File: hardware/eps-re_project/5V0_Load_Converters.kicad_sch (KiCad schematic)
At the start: 73 parts, among them Q10 EPC2016C, Q11 EPC2016C, Q12 EPC2016C, Q7 SI2302, Q8 SI2302, Q9 EPC2016C, U24 INA199C3DCKR

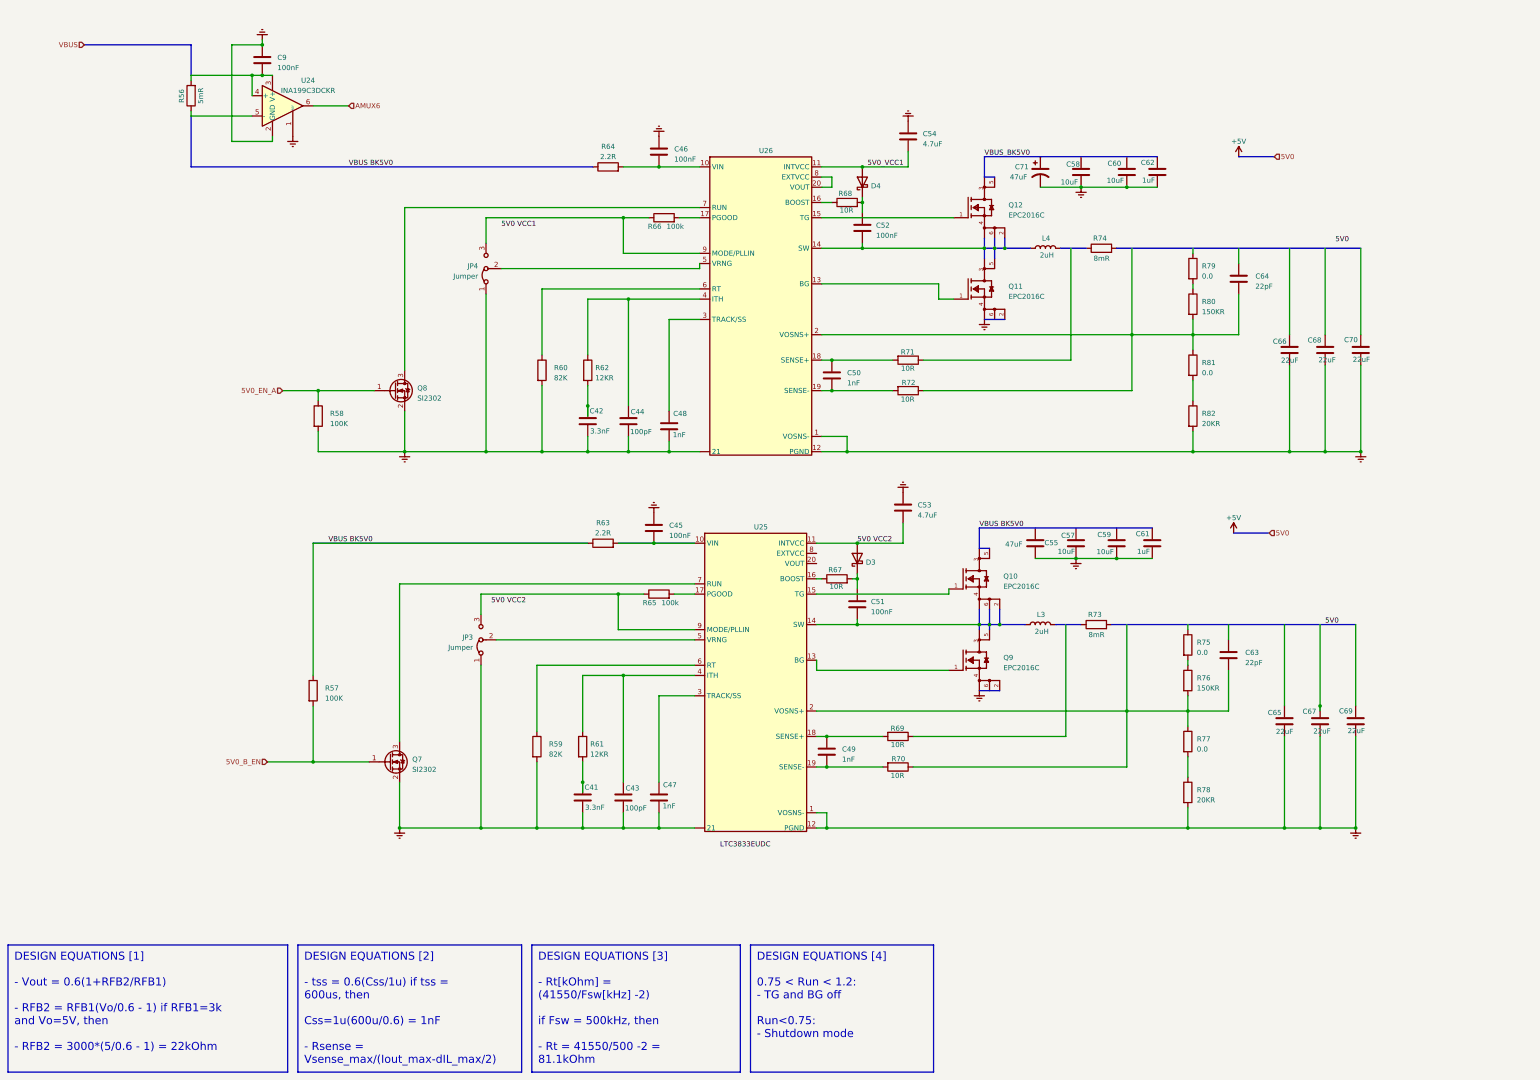
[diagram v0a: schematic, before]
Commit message: hardware: Restructuring the circuit, modifying symbols, footprints and other corrections
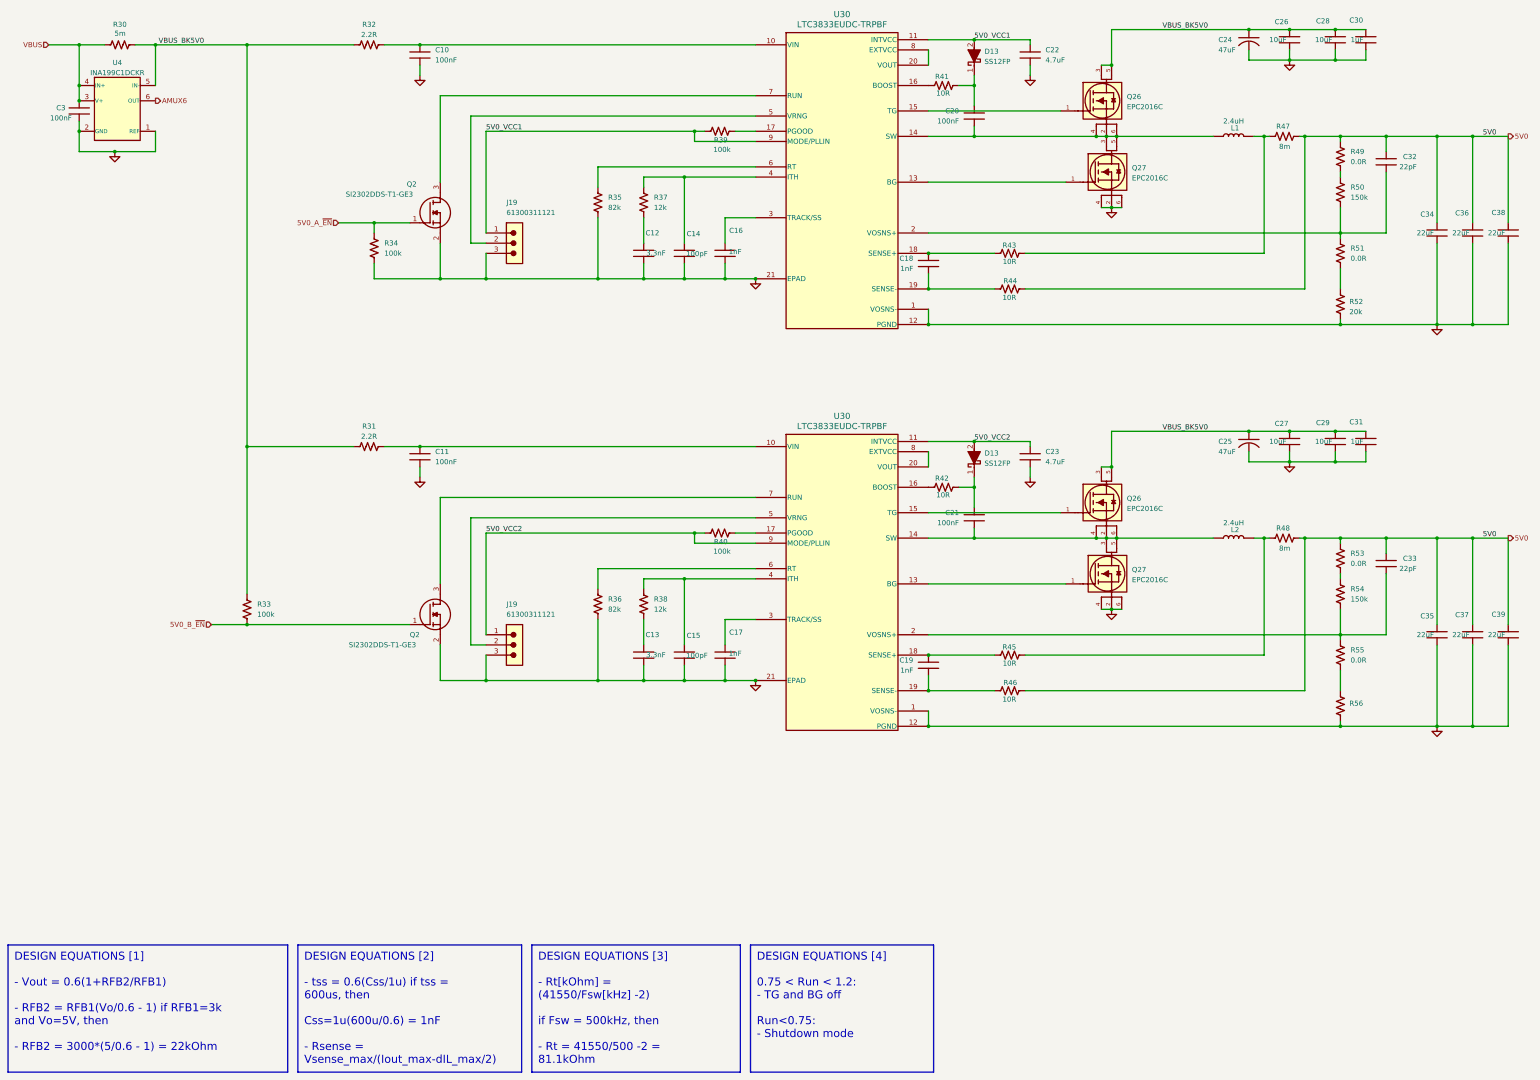
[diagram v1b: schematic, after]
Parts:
- removed C41, C42: 3.3nF, symbol Device:C
- removed C43, C44: 100pF, symbol Device:C
- removed C45, C46, C51, C52, C9: 100nF, symbol Device:C
- removed C47, C48, C49, C50: 1nF, symbol Device:C
- removed C53, C54: 4.7uF, symbol Device:C
- removed C55: 47uF, symbol Device:C
- removed C57, C58, C59, C60: 10uF, symbol Device:C
- removed C61, C62: 1uF, symbol Device:C
- removed C63, C64: 22pF, symbol Device:C
- removed C65, C66, C67, C68, C69, C70: 22uF, symbol Device:C
- removed C71: 47uF, symbol Device:C_Polarized_US
- removed D3, D4: ~, symbol Device:D_Schottky
- removed JP3, JP4: Jumper, symbol Jumper:Jumper_3_Bridged12
- removed L3, L4: 2uH, symbol Device:L
- removed Q10, Q11, Q12, Q9: EPC2016C, EPC-EPC2016C-*, symbol eec:EPC2016C
- removed Q7, Q8: SI2302, symbol Device:Q_NMOS_GSD
- removed R56: 5mR, symbol Device:R
- removed R57, R58: 100K, symbol Device:R
- removed R59, R60: 82K, symbol Device:R
- removed R61, R62: 12KR, symbol Device:R
- removed R63, R64: 2.2R, symbol Device:R
- removed R65, R66: 100k, symbol Device:R
- removed R67, R68, R69, R70, R71, R72: 10R, symbol Device:R
- removed R73, R74: 8mR, symbol Device:R
- removed R75, R77, R79, R81: 0.0, symbol Device:R
- removed R76, R80: 150KR, symbol Device:R
- removed R78, R82: 20KR, symbol Device:R
- removed U24: INA199C3DCKR, Package_TO_SOT_SMD:SOT-363_SC-70-6, symbol Amplifier_Current:INA199xxDCK
- removed U25, U26: ~, symbol New_Library:LTC3833EUDC
- added C10, C11, C20, C21, C3: 100nF, footprints:C0603C104K5RACTU, symbol C0603C104K5RACTU:C0603C104K5RACTU
- added C12, C13: 3.3nF, footprints:C0603C332J5GACAUTO, symbol C0603C332J5GACAUTO:C0603C332J5GACAUTO
- added C14, C15: 100pF, footprints:C0603C101J5GACAUTO, symbol C0603C101J5GACAUTO:C0603C101J5GACAUTO
- added C16, C17, C18, C19: 1nF, footprints:C0603C102F3GACTU, symbol C0603C102F3GACTU:C0603C102F3GACTU
- added C22, C23: 4.7uF, footprints:GCM32ER71H475KA55L, symbol GCM32ER71H475KA55L:GCM32ER71H475KA55L
- added C24, C25: 47uF, footprints:T495X476K035ATE300, symbol T495X476K035ATE300:T495X476K035ATE300
- added C26, C27, C28, C29: 10uF, footprints:C1210C106K5RACTU, symbol C1210C106K5RACTU:C1210C106K5RACTU
- added C30, C31: 1uF, footprints:C0805C105K5RACTU, symbol C0805C105K5RACTU:C0805C105K5RACTU
- added C32, C33: 22pF, footprints:C0603C220K5RACAUTO, symbol C0603C220K5RACAUTO:C0603C220K5RACAUTO
- added C34, C35, C36, C37, C38, C39: 22uF, footprints:GCM32ER71C226KE19L, symbol GCM32ER71C226KE19L:GCM32ER71C226KE19L
- added D13 (x2): SS12FP, footprints:SS12FP, symbol SS12FP:SS12FP
- added J19 (x2): 61300311121, footprints:61300311121, symbol 61300311121:61300311121
- added L1, L2: 2.4uH, footprints:744325240, symbol 744325240:744325240
- added Q2 (x2): SI2302DDS-T1-GE3, footprints:SI2302DDS-T1-GE3, symbol SI2302DDS-T1-GE3:SI2302DDS-T1-GE3
- added Q26 (x2), Q27 (x2): EPC2016C, footprints:EPC2016C, symbol EPC2016C:EPC2016C
- added R30: 5m, symbol Device:R_US
- added R31, R32: 2.2R, symbol Device:R_US
- added R33, R34, R39, R40: 100k, symbol Device:R_US
- added R35, R36: 82k, symbol Device:R_US
- added R37, R38: 12k, symbol Device:R_US
- added R41, R42, R43, R44, R45, R46: 10R, symbol Device:R_US
- added R47, R48: 8m, symbol Device:R_US
- added R49, R51, R53, R55: 0.0R, symbol Device:R_US
- added R50, R54: 150k, symbol Device:R_US
- added R52, R56: 20k, symbol Device:R_US
- added U30 (x2): LTC3833EUDC-TRPBF, footprints:LTC3833EUDC#TRPBF, symbol LTC3833EUDC#TRPBF:LTC3833EUDC-TRPBF
- added U4: INA199C1DCKR, footprints:INA199C1DCKR, symbol INA199C1DCKR:INA199xxDCK
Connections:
- net 5V0: now also C32.1, C33.1, C34.2, C35.2, C36.2, C37.2, C38.2, C39.2, R44.1, R46.1, R47.2, R48.2, R49.1, R53.1
- net 5V0_VCC1: now also C22.1, D13.2 (A), J19.1, R39.1, U30.11 (INTVCC), U30.9 (MODE/PLLIN)
- net AMUX6: now also U4.6 (OUT)
- net VBUS: now also C3.1, R30.1, U4.3 (V+), U4.4 (IN+)
- net VBUS_BK5V0: now also C24.2 (ANODE), C25.2 (ANODE), C26.1, C27.1, C28.1, C29.1, C30.1, C31.1, Q26.3 (Drain), Q26.3 (Drain), Q26.5 (Drain), Q26.5 (Drain), R30.2, R31.1, R32.1, R33.1, U4.5 (IN-)
- new net: C32.2, R50.2, R51.1, U30.2 (VOSNS+)
- new net: R51.2, R52.1
- new net: L1.2, R43.1, R47.1
- new net: L2.2, R45.1, R48.1
- new net: C11.2, R31.2, U30.10 (VIN)
- new net: Q27.1 (Gate), U30.13 (BG) (x2)
- new net: C21.2, L2.1, Q26.2 (Substrate), Q26.4 (Source), Q26.6 (Source), Q27.3 (Drain), Q27.5 (Drain), U30.14 (SW)
- new net: Q26.1 (Gate), U30.15 (TG) (x2)
- new net: R42.1, U30.16 (BOOST)
- new net: R40.2, U30.17 (PGOOD)
- new net: C19.1, R45.2, U30.18 (SENSE+)
- new net: C19.2, R46.2, U30.19 (SENSE-)
- new net: C33.2, R54.2, R55.1, U30.2 (VOSNS+)
- new net: U30.20 (VOUT), U30.8 (EXTVCC) (x2)
- new net: C17.1, U30.3 (TRACK/SS)
- new net: C15.1, R38.1, U30.4 (ITH)
- new net: J19.2, U30.5 (VRNG) (x2)
- new net: R36.1, U30.6 (RT)
- new net: Q2.3 (D), U30.7 (RUN) (x2)
- new net: C20.2, L1.1, Q26.2 (Substrate), Q26.4 (Source), Q26.6 (Source), Q27.3 (Drain), Q27.5 (Drain), U30.14 (SW)
- new net: C16.1, U30.3 (TRACK/SS)
- new net: C10.2, R32.2, U30.10 (VIN)
- new net: C18.2, R44.2, U30.19 (SENSE-)
- new net: C18.1, R43.2, U30.18 (SENSE+)
- new net: R55.2, R56.1
- new net: R49.2, R50.1
- new net: C13.1, R38.2
- new net: R39.2, U30.17 (PGOOD)
- new net: C21.1, D13.1 (K), R42.2
- new net: R53.2, R54.1
- new net: C20.1, D13.1 (K), R41.2
- new net: R41.1, U30.16 (BOOST)
- new net: C14.1, R37.1, U30.4 (ITH)
- new net: R35.1, U30.6 (RT)
- new net: C12.1, R37.2
- new net 5V0_A_~{EN}: Q2.1 (G), R34.1
- new net 5V0_B_~{EN}: Q2.1 (G), R33.2
- new net 5V0_VCC2: C23.1, D13.2 (A), J19.1, R40.1, U30.11 (INTVCC), U30.9 (MODE/PLLIN)
- new net GND: C10.1, C11.1, C12.2, C13.2, C14.2, C15.2, C16.2, C17.2, C22.2, C23.2, C24.1 (CATHODE), C25.1 (CATHODE), C26.2, C27.2, C28.2, C29.2, C3.2, C30.2, C31.2, C34.1, C35.1, C36.1, C37.1, C38.1, C39.1, J19.3, J19.3, Q2.2 (S), Q2.2 (S), Q27.2 (Substrate), Q27.2 (Substrate), Q27.4 (Source), Q27.4 (Source), Q27.6 (Source), Q27.6 (Source), R34.2, R35.2, R36.2, R52.2, R56.2, U30.1 (VOSNS-), U30.1 (VOSNS-), U30.12 (PGND), U30.12 (PGND), U30.21 (EPAD), U30.21 (EPAD), U4.1 (REF), U4.2 (GND)
